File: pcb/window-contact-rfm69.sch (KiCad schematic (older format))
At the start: 13 parts, among them IC1 ATMEGA328P-A, P1 REED, P2 AN

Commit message: updated kicad files
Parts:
- removed P1: REED, Pin_Headers:Pin_Header_Straight_1x03, symbol CONN_01X03
- added P1: VCC, wirepad:Wire_SMD_Pad_1PIN, symbol CONN_01X01
- added P2: TX/RX, Pin_Headers:Pin_Header_Straight_1x02, symbol CONN_01X02
- added P3: RE1, wirepad:Wire_SMD_Pad_1PIN, symbol CONN_01X01
- added P4: ISP, isp:SMD, symbol CONN_01X06
- added P5: RE2, wirepad:Wire_SMD_Pad_1PIN, symbol CONN_01X01
- added R3: 10M, Resistors_SMD:R_0805_HandSoldering, symbol R
- R2: footprint Resistors_ThroughHole:Resistor_Horizontal_RM10mm -> Resistors_SMD:R_0805_HandSoldering
- renumbered C2 to C1, C3 to C2, C1 to C3, P2 to P6, R3 to R4, R4 to R5, R5 to R6
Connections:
- net GND: now also P4.6 (P6), R3.2
- net MISO: now also P4.1 (P1)
- net MOSI: now also P4.4 (P4)
- net SCK: now also P4.3 (P3)
- net VCC: now also P1.1 (P1), P4.2 (P2)
- net at R2.1: now also IC1.24 ((PCINT9/ADC1)PC1), P3.1 (P1)
- net at IC1.29 ((PCINT14/~RESET~)PC6), R1.2: now also P4.5 (P5)
- net at IC1.23 ((PCINT8/ADC0)PC0): now also P5.1 (P1), R3.1
- net at IC1.30 ((PCINT16/RXD)PD0): now also P2.1 (P1)
- net at IC1.31 ((PCINT17/TXD)PD1): now also P2.2 (P2)
- no-connect marks 8 -> 21
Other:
- moved on the sheet: R2
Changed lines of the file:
@@
 $EndComp
 $Comp
-L C C1
+L C C3
 U 1 1 5B016625
 P 2100 5150
-F 0 "C1" H 2125 5250 50  0000 L CNN
+F 0 "C3" H 2125 5250 50  0000 L CNN
 F 1 "100nf" H 2125 5050 50  0000 L CNN
 F 2 "Capacitors_SMD:C_0805_HandSoldering" H 2138 5000 50  0001 C CNN
@@
 L R R2
 U 1 1 5B01665D
-P 5100 3700
-F 0 "R2" V 5180 3700 50  0000 C CNN
-F 1 "10M" V 5100 3700 50  0000 C CNN
-F 2 "Resistors_ThroughHole:Resistor_Horizontal_RM10mm" V 5030 3700 50  0001 C CNN
-F 3 "" H 5100 3700 50  0000 C CNN
-	1    5100 3700
+P 5250 7200
+F 0 "R2" V 5330 7200 50  0000 C CNN
+F 1 "10M" V 5250 7200 50  0000 C CNN
+F 2 "Resistors_SMD:R_0805_HandSoldering" V 5180 7200 50  0001 C CNN
+F 3 "" H 5250 7200 50  0000 C CNN
+	1    5250 7200
 	1    0    0    -1
 $EndComp
@@
 Text GLabel 1900 1200 2    60   Input ~ 0
 VCC
-Text GLabel 5550 3750 0    60   Input ~ 0
-VCC
-$Comp
-L CONN_01X03 P1
-U 1 1 5B017A1A
-P 5900 3650
-F 0 "P1" H 5900 3850 50  0000 C CNN
-F 1 "REED" V 6000 3650 50  0000 C CNN
-F 2 "Pin_Headers:Pin_Header_Straight_1x03" H 5900 3650 50  0001 C CNN
-F 3 "" H 5900 3650 50  0000 C CNN
-	1    5900 3650
-	1    0    0    -1
-$EndComp
-Wire Wire Line
-	5700 3750 5550 3750
-NoConn ~ 5700 3650
-Connection ~ 5100 3550
-Text GLabel 5100 3950 3    60   Input ~ 0
-GND
-Wire Wire Line
-	5100 3850 5100 3950
-$Comp
-L CP C2
+$Comp
+L CP C1
 U 1 1 5B018A0C
 P 1650 1350
-F 0 "C2" H 1675 1450 50  0000 L CNN
+F 0 "C1" H 1675 1450 50  0000 L CNN
 F 1 "10uF" H 1675 1250 50  0000 L CNN
 F 2 "Capacitors_SMD:c_elec_4x5.8" H 1688 1200 50  0001 C CNN
@@
 NoConn ~ 2300 5050
 $Comp
-L C C3
+L C C2
 U 1 1 5B13F6B2
 P 2000 4650
-F 0 "C3" H 2025 4750 50  0000 L CNN
+F 0 "C2" H 2025 4750 50  0000 L CNN
 F 1 "100nf" H 2025 4550 50  0000 L CNN
 F 2 "Capacitors_SMD:C_0805_HandSoldering" H 2038 4500 50  0001 C CNN
@@
 NoConn ~ 2300 5900
 $Comp
-L R R5
+L R R6
 U 1 1 5B140033
 P 8800 5000
-F 0 "R5" V 8880 5000 50  0000 C CNN
+F 0 "R6" V 8880 5000 50  0000 C CNN
 F 1 "1k" V 8800 5000 50  0000 C CNN
 F 2 "Resistors_SMD:R_0805_HandSoldering" V 8730 5000 50  0001 C CNN
@@
 Wire Wire Line
 	4550 5900 4200 5900
-Wire Wire Line
-	5700 3550 5100 3550
 Text GLabel 8600 5300 2    60   Input ~ 0
 VCC
@@
 	8200 5200 8950 5200
 $Comp
-L CONN_01X01 P2
+L CONN_01X01 P6
 U 1 1 5B140A1B
 P 8600 5600
-F 0 "P2" H 8600 5700 50  0000 C CNN
+F 0 "P6" H 8600 5700 50  0000 C CNN
 F 1 "AN" V 8700 5600 50  0000 C CNN
 F 2 "Wire_Pads:SolderWirePad_single_1mmDrill" H 8600 5600 50  0001 C CNN
@@
 NoConn ~ 7200 5100
 $Comp
-L R R4
+L R R5
 U 1 1 5B140CDD
 P 8500 4900
-F 0 "R4" V 8580 4900 50  0000 C CNN
+F 0 "R5" V 8580 4900 50  0000 C CNN
 F 1 "1k" V 8500 4900 50  0000 C CNN
 F 2 "Resistors_SMD:R_0805_HandSoldering" V 8430 4900 50  0001 C CNN
@@
 $EndComp
 $Comp
-L R R3
+L R R4
 U 1 1 5B140D43
 P 6900 4800
-F 0 "R3" V 6980 4800 50  0000 C CNN
+F 0 "R4" V 6980 4800 50  0000 C CNN
 F 1 "1k" V 6900 4800 50  0000 C CNN
 F 2 "Resistors_SMD:R_0805_HandSoldering" V 6830 4800 50  0001 C CNN
@@
 Text Label 8950 4900 0    60   ~ 0
 MOSI
+$Comp
+L CONN_01X06 P4
+U 1 1 5B19650E
+P 6300 3400
+F 0 "P4" H 6300 3750 50  0000 C CNN
+F 1 "ISP" V 6400 3400 50  0000 C CNN
+F 2 "isp:SMD" H 6300 3400 50  0001 C CNN
+F 3 "" H 6300 3400 50  0000 C CNN
+	1    6300 3400
+	0    -1   -1   0
+$EndComp
+NoConn ~ 7200 5000
+Entry Wire Line
+	6300 4450 6400 4550
+Entry Wire Line
+	6200 4450 6300 4550
+Entry Wire Line
+	6050 4450 6150 4550
+Text GLabel 6550 3750 3    60   Input ~ 0
+GND
+Text GLabel 6150 3750 3    60   Input ~ 0
+VCC
+Wire Wire Line
+	6150 3600 6150 3750
+Wire Wire Line
+	6550 3600 6550 3750
+Wire Wire Line
+	6450 3600 6450 5600
+Wire Wire Line
+	6450 5600 4500 5600
+Wire Wire Line
+	4500 5600 4500 5900
+Connection ~ 4500 5900
+Wire Wire Line
+	6300 4450 6350 4450
+Wire Wire Line
+	6350 4450 6350 3600
+Wire Wire Line
+	6200 4450 6200 4100
+Wire Wire Line
+	6200 4100 6250 4100
+Wire Wire Line
+	6250 4100 6250 3600
+Wire Wire Line
+	6050 4450 6050 3600
+Text Label 6050 4100 3    60   ~ 0
+MISO
+Text Label 6200 4250 1    60   ~ 0
+SCK
+Text Label 6350 4250 1    60   ~ 0
+MOSI
+$Comp
+L CONN_01X01 P5
+U 1 1 5B197BA2
+P 6350 6650
+F 0 "P5" H 6350 6750 50  0000 C CNN
+F 1 "RE2" V 6450 6650 50  0000 C CNN
+F 2 "wirepad:Wire_SMD_Pad_1PIN" H 6350 6650 50  0001 C CNN
+F 3 "" H 6350 6650 50  0000 C CNN
+	1    6350 6650
+	1    0    0    -1
+$EndComp
+$Comp
+L CONN_01X01 P3
+U 1 1 5B197C31
+P 5600 7050
+F 0 "P3" H 5600 7150 50  0000 C CNN
+F 1 "RE1" V 5700 7050 50  0000 C CNN
+F 2 "wirepad:Wire_SMD_Pad_1PIN" H 5600 7050 50  0001 C CNN
+F 3 "" H 5600 7050 50  0000 C CNN
+	1    5600 7050
+	1    0    0    -1
+$EndComp
+$Comp
+L CONN_01X01 P1
+U 1 1 5B197CCB
+P 1800 2100
+F 0 "P1" H 1800 2200 50  0000 C CNN
+F 1 "VCC" V 1900 2100 50  0000 C CNN
+F 2 "wirepad:Wire_SMD_Pad_1PIN" H 1800 2100 50  0001 C CNN
+F 3 "" H 1800 2100 50  0000 C CNN
+	1    1800 2100
+	1    0    0    -1
+$EndComp
+Text GLabel 1500 2100 0    60   Input ~ 0
+VCC
+Wire Wire Line
+	1600 2100 1500 2100
+$Comp
+L R R3
+U 1 1 5B1981B6
+P 6000 6800
+F 0 "R3" V 6080 6800 50  0000 C CNN
+F 1 "10M" V 6000 6800 50  0000 C CNN
+F 2 "Resistors_SMD:R_0805_HandSoldering" V 5930 6800 50  0001 C CNN
+F 3 "" H 6000 6800 50  0000 C CNN
+	1    6000 6800
+	1    0    0    -1
+$EndComp
+Text GLabel 6000 7100 3    60   Input ~ 0
+GND
+Text GLabel 5250 7450 3    60   Input ~ 0
+GND
+Wire Wire Line
+	5250 7350 5250 7450
+Wire Wire Line
+	5250 7050 5400 7050
+Wire Wire Line
+	6000 7100 6000 6950
+Wire Wire Line
+	5700 6650 6150 6650
+Wire Wire Line
+	4200 5300 5700 5300
+Wire Wire Line
+	5700 5300 5700 6650
+Connection ~ 6000 6650
+Wire Wire Line
+	4200 5400 5400 5400
+Wire Wire Line
+	5400 5400 5400 6900
+Wire Wire Line
+	5400 6900 5250 6900
+Wire Wire Line
+	5250 6900 5250 7050
+NoConn ~ 4200 4450
+NoConn ~ 4200 4550
+NoConn ~ 4200 5050
+NoConn ~ 4200 5150
+NoConn ~ 4200 5500
+NoConn ~ 4200 5600
+NoConn ~ 4200 5700
+NoConn ~ 4200 5800
+NoConn ~ 4200 6350
+NoConn ~ 4200 6450
+NoConn ~ 4200 6550
+NoConn ~ 4200 6650
+NoConn ~ 4200 6750
+$Comp
+L CONN_01X02 P2
+U 1 1 5B19964F
+P 4950 6150
+F 0 "P2" H 4950 6300 50  0000 C CNN
+F 1 "TX/RX" V 5050 6150 50  0000 C CNN
+F 2 "Pin_Headers:Pin_Header_Straight_1x02" H 4950 6150 50  0001 C CNN
+F 3 "" H 4950 6150 50  0000 C CNN
+	1    4950 6150
+	1    0    0    -1
+$EndComp
+Wire Wire Line
+	4750 6100 4400 6100
+Wire Wire Line
+	4400 6100 4400 6050
+Wire Wire Line
+	4400 6050 4200 6050
+Wire Wire Line
+	4200 6150 4350 6150
+Wire Wire Line
+	4350 6150 4350 6200
+Wire Wire Line
+	4350 6200 4750 6200
 $EndSCHEMATC

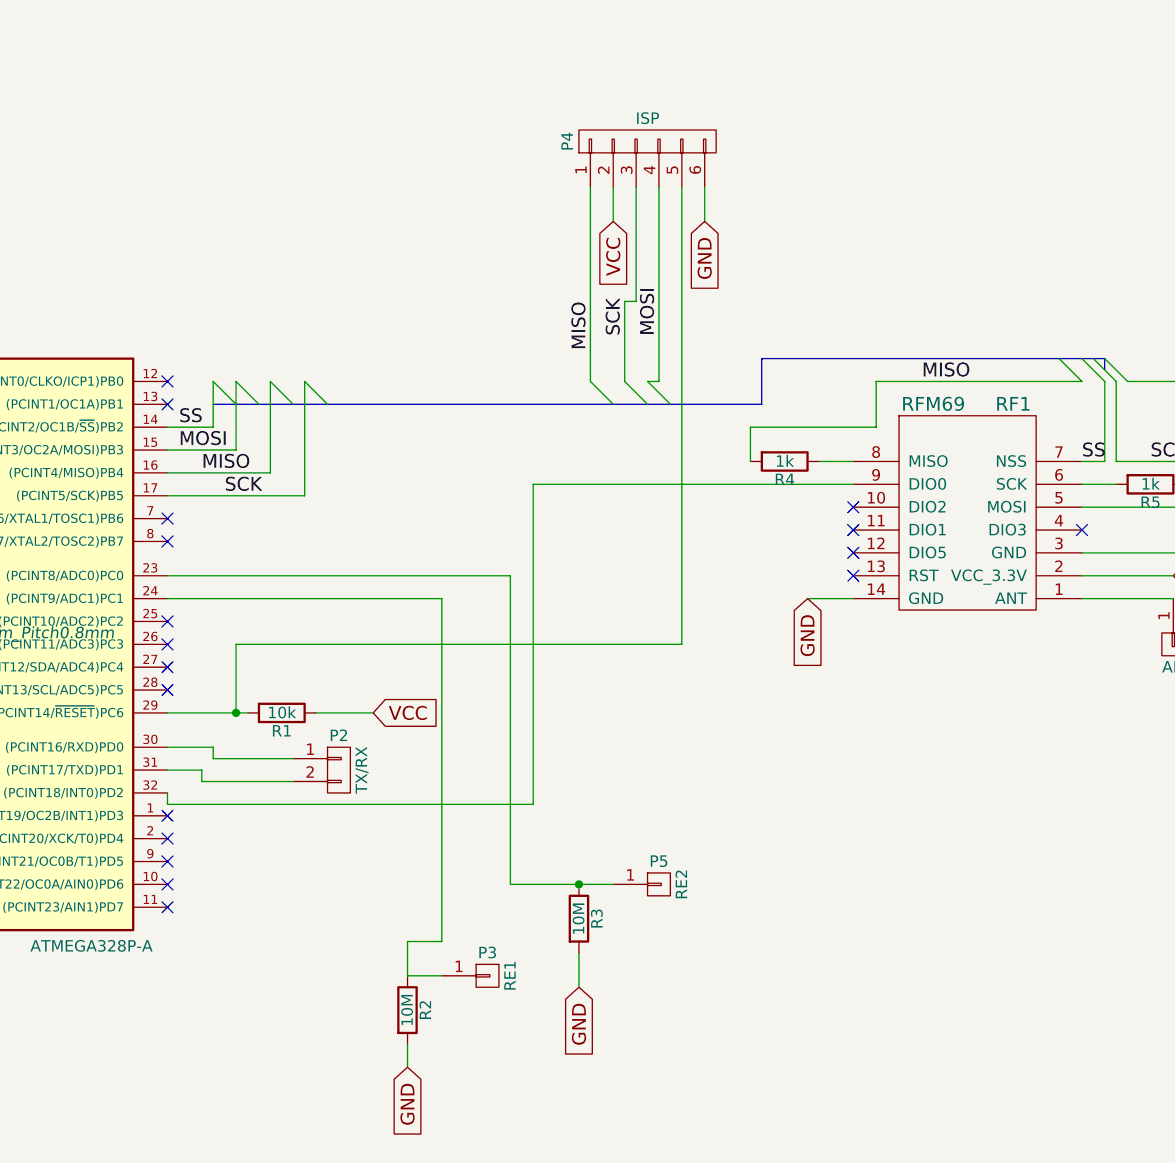
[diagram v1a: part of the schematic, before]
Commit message: added Status LEDs and Debug Push Button
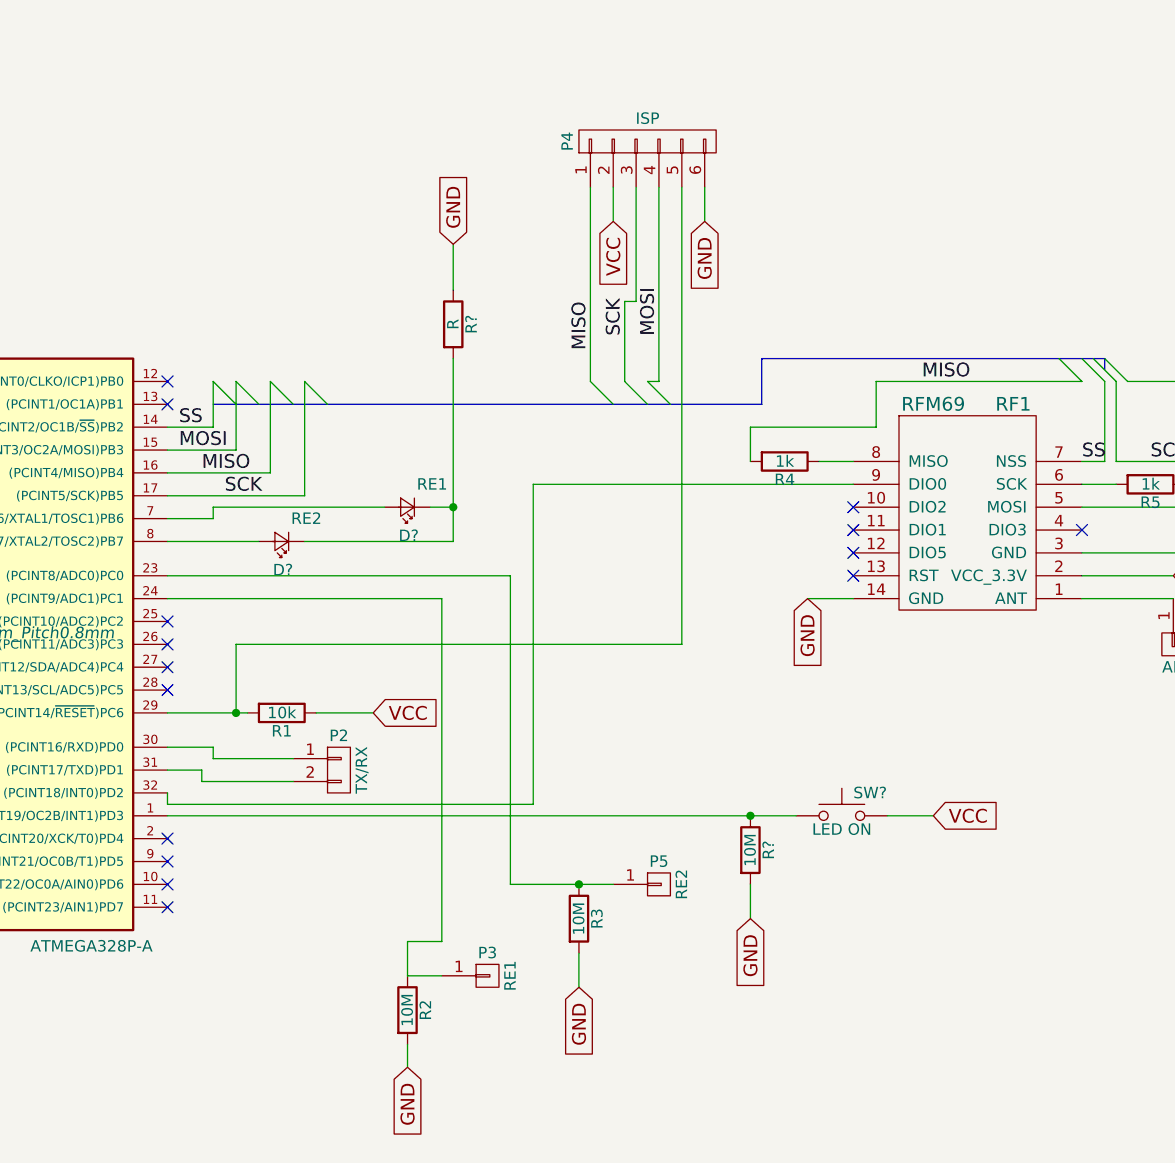
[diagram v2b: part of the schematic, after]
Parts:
- added D?: RE1, symbol LED_Small
- added D?: RE2, symbol LED_Small
- added R?: 10M, Resistors_SMD:R_0805_HandSoldering, symbol R
- added R?: R, symbol R
- added SW?: LED ON, symbol SW_Push
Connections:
- net GND: now also R?.1, R?.2
- net VCC: now also SW?.2
- net at IC1.1 ((PCINT19/OC2B/INT1)PD3): now also R?.1, SW?.1
- net at IC1.7 ((PCINT6/XTAL1/TOSC1)PB6): now also D?.2 (A)
- net at IC1.8 ((PCINT7/XTAL2/TOSC2)PB7): now also D?.2 (A)
- new net: D?.1 (K), D?.1 (K), R?.2
- no-connect marks 21 -> 18
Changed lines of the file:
@@
 LIBS:valves
 LIBS:rfm69
+LIBS:Switch
 LIBS:window-contact-rfm69-cache
 EELAYER 25 0
@@
 NoConn ~ 4200 4450
 NoConn ~ 4200 4550
-NoConn ~ 4200 5050
-NoConn ~ 4200 5150
 NoConn ~ 4200 5500
 NoConn ~ 4200 5600
 NoConn ~ 4200 5700
 NoConn ~ 4200 5800
-NoConn ~ 4200 6350
 NoConn ~ 4200 6450
 NoConn ~ 4200 6550
@@
 Wire Wire Line
 	4350 6200 4750 6200
+$Comp
+L R R?
+U 1 1 5B891AA9
+P 6750 6500
+F 0 "R?" V 6830 6500 50  0000 C CNN
+F 1 "10M" V 6750 6500 50  0000 C CNN
+F 2 "Resistors_SMD:R_0805_HandSoldering" V 6680 6500 50  0001 C CNN
+F 3 "" H 6750 6500 50  0000 C CNN
+	1    6750 6500
+	1    0    0    -1
+$EndComp
+Text GLabel 6750 6800 3    60   Input ~ 0
+GND
+Wire Wire Line
+	4200 6350 6950 6350
+Wire Wire Line
+	6750 6650 6750 6800
+$Comp
+L SW_Push SW?
+U 1 1 5B8920C1
+P 7150 6350
+F 0 "SW?" H 7200 6450 50  0000 L CNN
+F 1 "LED ON" H 7150 6290 50  0000 C CNN
+F 2 "" H 7150 6550 50  0001 C CNN
+F 3 "" H 7150 6550 50  0001 C CNN
+	1    7150 6350
+	1    0    0    -1
+$EndComp
+Text GLabel 7550 6350 2    60   Input ~ 0
+VCC
+Wire Wire Line
+	7350 6350 7550 6350
+Connection ~ 6750 6350
+$Comp
+L R R?
+U 1 1 5B892B3A
+P 5450 4200
+F 0 "R?" V 5530 4200 50  0000 C CNN
+F 1 "R" V 5450 4200 50  0000 C CNN
+F 2 "" V 5380 4200 50  0000 C CNN
+F 3 "" H 5450 4200 50  0000 C CNN
+	1    5450 4200
+	1    0    0    -1
+$EndComp
+Text GLabel 5450 3850 1    60   Input ~ 0
+GND
+Wire Wire Line
+	5450 3850 5450 4050
+$Comp
+L LED_Small D?
+U 1 1 5B892EF0
+P 5250 5000
+F 0 "D?" H 5200 5125 50  0000 L CNN
+F 1 "RE1" H 5075 4900 50  0000 L CNN
+F 2 "" V 5250 5000 50  0000 C CNN
+F 3 "" V 5250 5000 50  0000 C CNN
+	1    5250 5000
+	-1   0    0    1
+$EndComp
+$Comp
+L LED_Small D?
+U 1 1 5B8932F8
+P 4700 5150
+F 0 "D?" H 4650 5275 50  0000 L CNN
+F 1 "RE2" H 4525 5050 50  0000 L CNN
+F 2 "" V 4700 5150 50  0000 C CNN
+F 3 "" V 4700 5150 50  0000 C CNN
+	1    4700 5150
+	-1   0    0    1
+$EndComp
+Wire Wire Line
+	5150 5000 4400 5000
+Wire Wire Line
+	4400 5000 4400 5050
+Wire Wire Line
+	4400 5050 4200 5050
+Wire Wire Line
+	4200 5150 4600 5150
+Wire Wire Line
+	5450 5150 4800 5150
+Connection ~ 5450 5000
+Wire Wire Line
+	5450 4350 5450 5150
+Wire Wire Line
+	5450 5000 5350 5000
 $EndSCHEMATC
